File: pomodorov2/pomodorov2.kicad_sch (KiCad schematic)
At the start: 12 parts, among them J1 USB_B_Micro, J2 TC2050-IDC, J3 SOICbite, U1 MDBT50Q-1MV2, Y1 32.768kHz

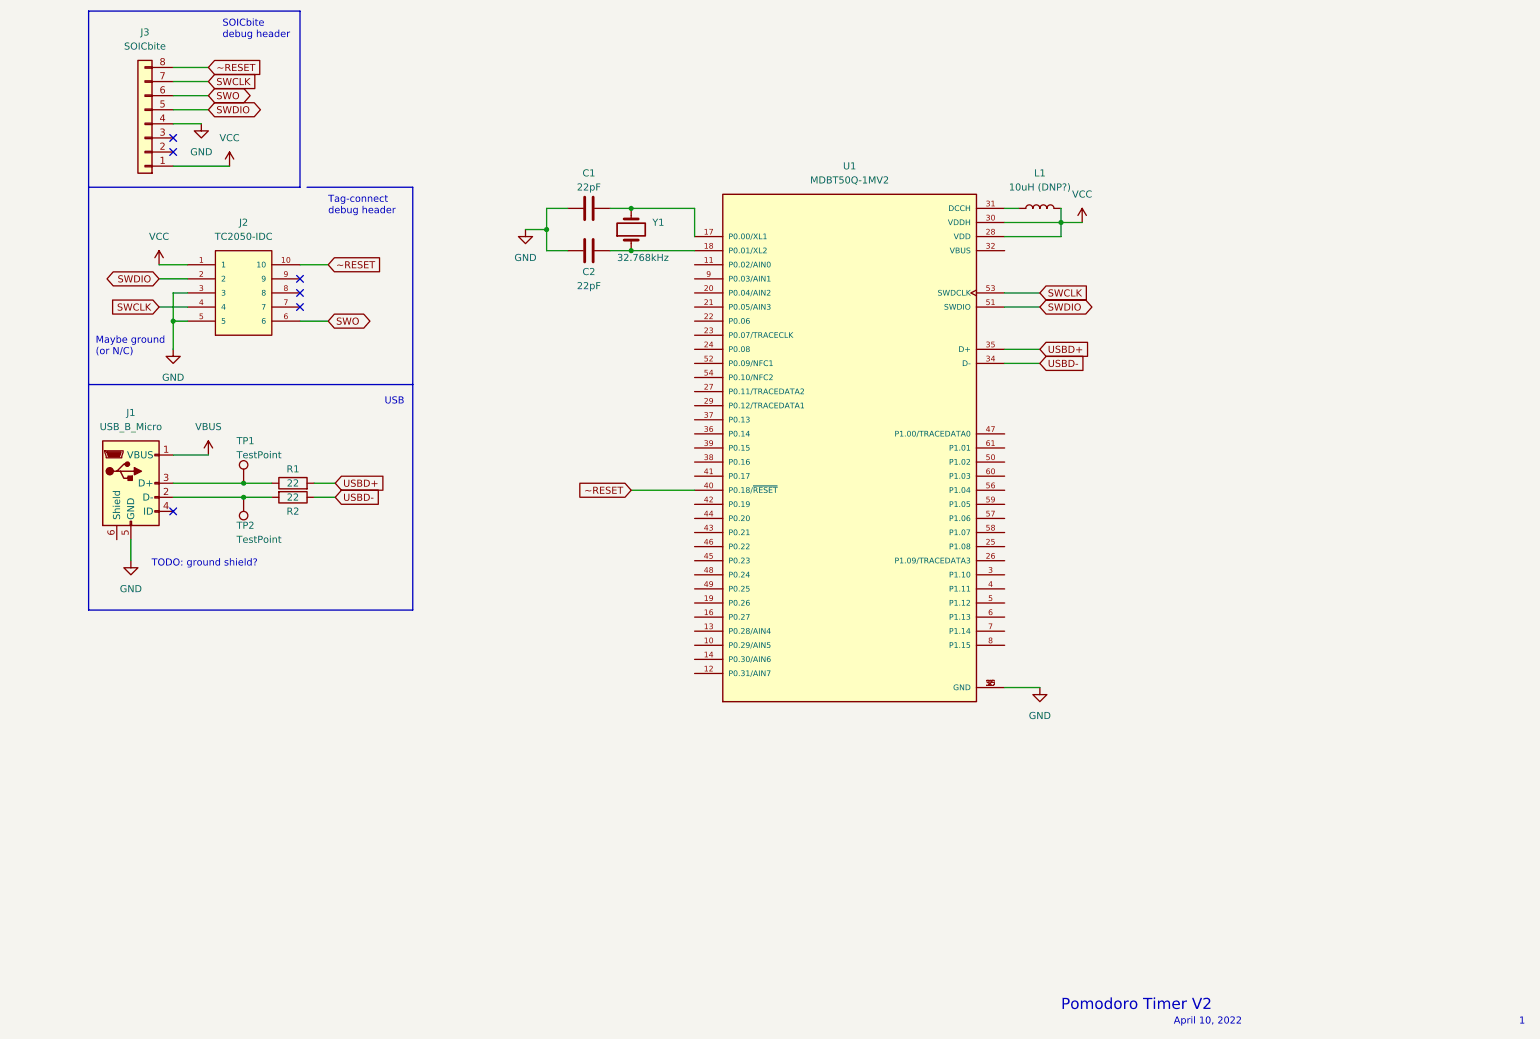
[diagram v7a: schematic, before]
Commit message: Add Stemma connector, add signals 📶
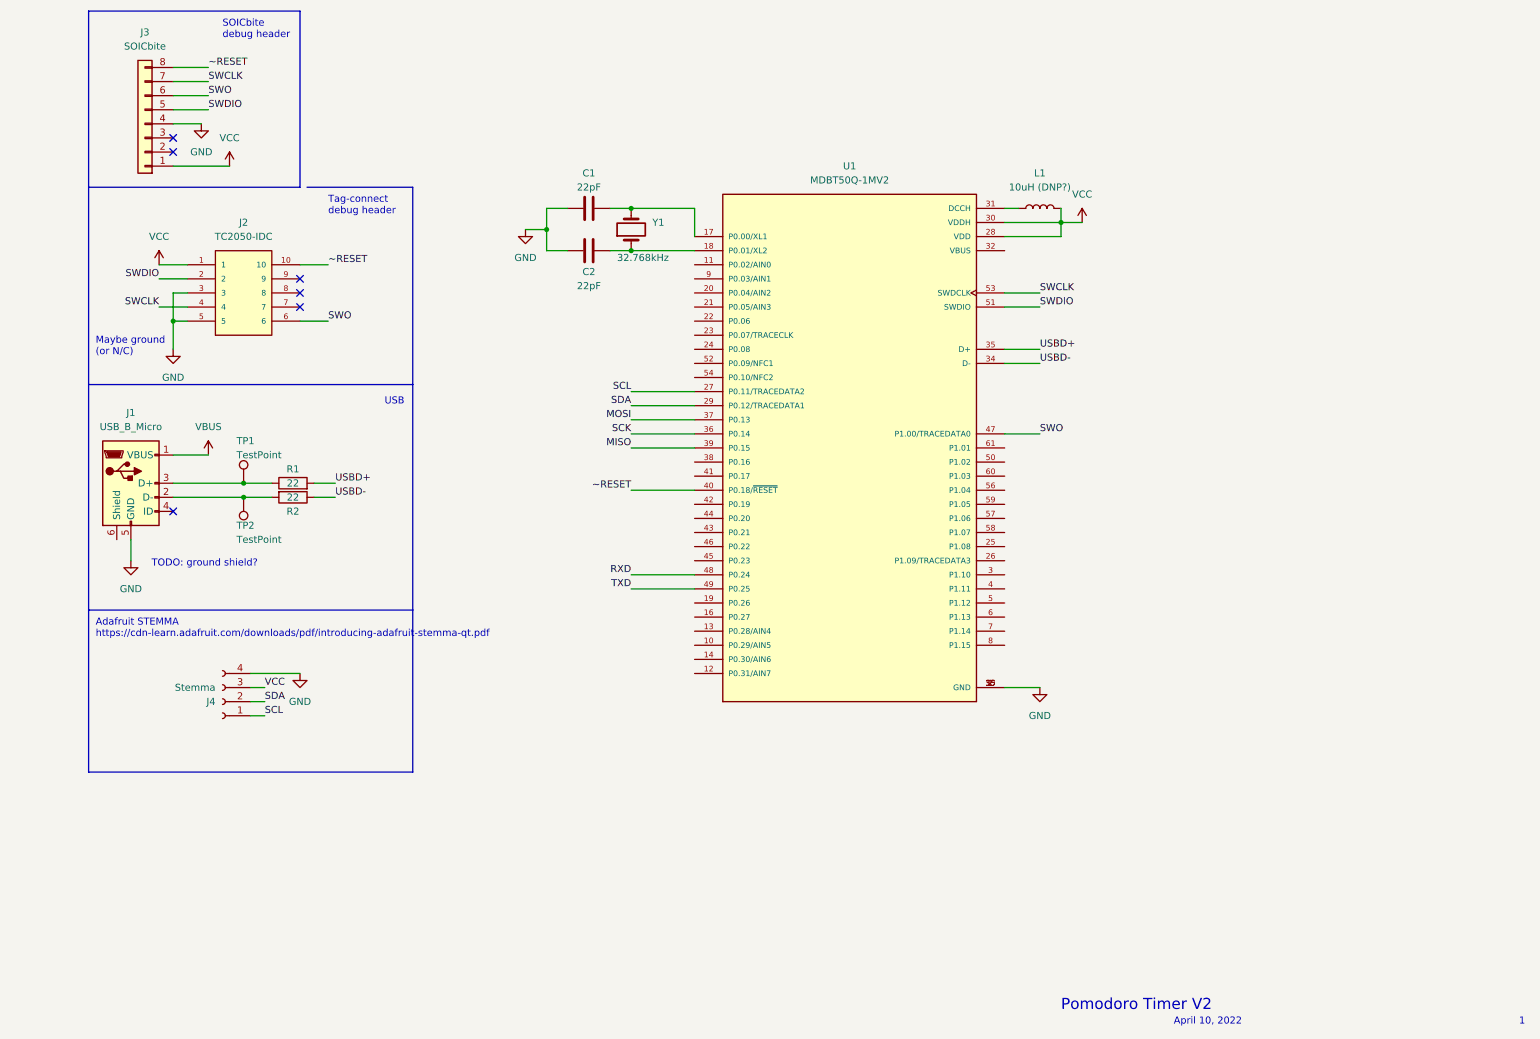
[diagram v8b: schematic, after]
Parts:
- added J4: Stemma, Connector_JST:JST_PH_S4B-PH-K_1x04_P2.00mm_Horizontal, symbol Connector:Conn_01x04_Female
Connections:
- net GND: now also J4.4 (Pin_4)
- net SWO: now also U1.47 (P1.00/TRACEDATA0)
- net VCC: now also J4.3 (Pin_3)
- net SCL: now reaches U1.27 (P0.11/TRACEDATA2)
- net SCL: now also J4.1 (Pin_1)
- net SDA: now reaches U1.29 (P0.12/TRACEDATA1)
- net SDA: now also J4.2 (Pin_2)
- net SCK: now reaches U1.36 (P0.14)
- net MOSI: now reaches U1.37 (P0.13)
- net MISO: now reaches U1.39 (P0.15)
- net RXD: now reaches U1.48 (P0.24)
- net TXD: now reaches U1.49 (P0.25)
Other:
- note added: "Adafruit STEMMA https://cdn-learn.adafruit.com/downloads/pdf/introducing-adafruit-stemma-qt.pdf"
